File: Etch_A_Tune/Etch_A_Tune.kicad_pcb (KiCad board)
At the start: 2 copper layers, 114.2 x 101.6 mm, 21 parts, among them IC1 STM32H7A3ZIT6, IC2 TPS62063DSGR, IC3 BQ29702DSER, IC4 LM2775DSGR, IC5 BQ25170DSGR, IC6 TLV320DAC3100IRHBR, J1 TSM-115-01-T-DV-P-TR, J2 TSM-110-01-T-DV-P, J3 UJ20-C-H-G-MSMT-2-P16-TR, J4 TSM-117-01-F-DV-P-TR, J5 TSM-108-01-L-DV-A-P-TR, U1 1042P, U2 RIC11-31S10K2-GSMT, U3 RIC11-31S10K2-GSMT

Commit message: Schematic Update
Fixed component Footprints and added new switches/rotary encoders. Wired and placed bypass capacitors for most devices. Removed 5V boost converter because external DAC is no longer being utilized. Placed uC onto board design and implemented charging through USB-C connector.
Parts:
- removed IC2: TPS62063DSGR, SamacSys:SON50P200X200X80-9N
- removed IC3: BQ29702DSER, SamacSys:TPS3710QDSERQ1
- removed IC4: LM2775DSGR, SamacSys:SON50P200X200X80-9N
- removed IC5: BQ25170DSGR, SamacSys:SON50P200X200X80-9N
- removed IC6: TLV320DAC3100IRHBR, SamacSys:QFN50P500X500X100-33N-D
- removed J1: TSM-115-01-T-DV-P-TR, SamacSys:TSM-115-YY-ZZZ-DV-P-TR
- removed J3: UJ20-C-H-G-MSMT-2-P16-TR, SamacSys:UJ20CHGMSMT2P16TR
- removed J4: TSM-117-01-F-DV-P-TR, SamacSys:TSM-117-YY-ZZZ-DV-P-TR
- removed J5: TSM-108-01-L-DV-A-P-TR, SamacSys:TSM-108-YY-ZZZ-DV-A-P-TR
- removed J?: SJ2-35853A-SMT-TR, SamacSys:SJ235853ASMTTR
- removed U2: RIC11-31S10K2-GSMT, SamacSys:RIC1131S10K2GSMT
- added BT1: 1042P, BQ25170DSGR:BAT_1042P, B.Cu at (134.0, 50.0)
- added MT1: RIC11-31S15D7-GSMT, BQ25170DSGR:XDCR_RIC11-31S15D7-GSMT, F.Cu at (311.5, 76.5)
- added MT2: RIC11-31S15D7-GSMT, BQ25170DSGR:XDCR_RIC11-31S15D7-GSMT, F.Cu at (397.5, 76.5)
- added TP1: TestPoint, TestPoint:TestPoint_Pad_D1.0mm, F.Cu at (330.6, 37.5)
- added TP10: TestPoint, TestPoint:TestPoint_Pad_D1.0mm, F.Cu at (338.0, 46.1)
- added TP11: TestPoint, TestPoint:TestPoint_Pad_D1.0mm, F.Cu at (341.1, 37.0)
- added TP12: TestPoint, TestPoint:TestPoint_Pad_D1.0mm, F.Cu at (341.1, 40.0)
- added TP13: TestPoint, TestPoint:TestPoint_Pad_D1.0mm, F.Cu at (341.1, 43.0)
- added TP2: TestPoint, TestPoint:TestPoint_Pad_D1.0mm, F.Cu at (330.6, 44.5)
- added TP3: TestPoint, TestPoint:TestPoint_Pad_D1.0mm, F.Cu at (330.1, 41.0)
- added TP4: TestPoint, TestPoint:TestPoint_Pad_D1.0mm, F.Cu at (346.5, 44.0)
- added TP5: TestPoint, TestPoint:TestPoint_Pad_D1.0mm, F.Cu at (346.1, 37.0)
- added TP6: TestPoint, TestPoint:TestPoint_Pad_D1.0mm, F.Cu at (346.1, 40.0)
- added TP7: TestPoint, TestPoint:TestPoint_Pad_D1.0mm, F.Cu at (338.0, 37.0)
- added TP8: TestPoint, TestPoint:TestPoint_Pad_D1.0mm, F.Cu at (338.0, 40.0)
- added TP9: TestPoint, TestPoint:TestPoint_Pad_D1.0mm, F.Cu at (338.0, 43.0)
- added U4: STM32H7A3ZIT6Q, BQ25170DSGR:LQFP-144-L, F.Cu at (132.2, 64.8)
- added U6: CSD16406Q3, BQ25170DSGR:TRANS_CSD16406Q3, F.Cu at (315.0, 99.2)
- added U7: CSD16406Q3, BQ25170DSGR:TRANS_CSD16406Q3, F.Cu at (315.0, 104.0)
- IC1: value STM32H7A3ZIT6 -> BQ25170DSGR; footprint SamacSys:QFP50P2200X2200X160-144N -> BQ25170DSGR:SON50P200X200X80-9N
- J2: value TSM-110-01-T-DV-P -> 2171790001; footprint SamacSys:TSM-110-YY-ZZZ-DV-P -> BQ25170DSGR:MOLEX_2171790001
- S1: footprint SamacSys:450404015514 -> BQ25170DSGR:450404015514
- S2, S3, S4, S5, S6: value PTS647SM70SMTR2LFS -> B3AL-1005P; footprint SamacSys:PTS647SM38SMTR2LFS -> BQ25170DSGR:B3AL1005P
- U1: value 1042P -> BQ297xy; footprint SamacSys:1042P -> Package_SON:WSON-6_1.5x1.5mm_P0.5mm; moved to F.Cu
- U3: value RIC11-31S10K2-GSMT -> TPS62063DSGR; footprint SamacSys:RIC1131S10K2GSMT -> BQ25170DSGR:DSG0008A
- moved S3 235.5 mm to (342.5, 85.0), turned to 90 degrees
- moved S4 235.4 mm to (352.5, 85.0), turned to 90 degrees
- moved S5 235.2 mm to (362.5, 85.0), turned to 90 degrees
- moved S6 234.6 mm to (372.0, 85.0), turned to 90 degrees
- moved U3 222.4 mm to (314.5, 107.8)
- moved U1 200.7 mm to (338.5, 111.2)
- moved IC1 191.1 mm to (333.0, 111.2)
- moved S2 187.1 mm to (332.5, 85.0), turned to 90 degrees
- moved J2 123.6 mm to (80.2, 43.2), turned to -90 degrees
- moved S1 63.0 mm to (185.0, 40.0)
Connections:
- IC1 pad 1: (no net) -> /Battery/USB_Power
- IC1 pad 2: (no net) -> Net-(IC1-ISET)
- IC1 pad 3: (no net) -> Net-(IC1-TS)
- IC1 pad 4: (no net) -> GND
- IC1 pad 5: (no net) -> /Battery/BAT_DIAG
- IC1 pad 6: (no net) -> /Battery/PG
- IC1 pad 7: (no net) -> GND
- IC1 pad 8: (no net) -> /Battery/Power
- IC1 pad 9: (no net) -> GND
- S1 pad 1: (no net) -> Net-(R1-Pad1)
- S1 pad 2: (no net) -> /Controllers/SlideSwitch
- S1 pad 3: (no net) -> GND
- S2 pad 1: (no net) -> /Controllers/SW1
- S2 pad 2: (no net) -> GND
- S3 pad 1: (no net) -> /Controllers/SW2
- S3 pad 2: (no net) -> GND
- S4 pad 1: (no net) -> /Controllers/SW3
- S4 pad 2: (no net) -> GND
- S5 pad 1: (no net) -> /Controllers/SW4
- S5 pad 2: (no net) -> GND
- S6 pad 1: (no net) -> /Controllers/SW5
- S6 pad 2: (no net) -> GND
- U1 pad 1: (no net) -> unconnected-(U1-NC-Pad1)
- U1 pad 2: (no net) -> Net-(U1-Cout)
- U1 pad 3: (no net) -> Net-(U1-Dout)
- U1 pad 4: (no net) -> GND
- U1 pad 5: (no net) -> Net-(U1-BAT)
- U3 pad 1: (no net) -> GND
- U3 pad 2: (no net) -> Net-(U3-SW)

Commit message: Etch A Tune V.02
Updated more foot prints and components onto bom, specifically SWD debug header and 1x14 pin header for touch and screen module. Added 4pin header for SD card reader.
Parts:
- removed U6, U7: CSD16406Q3, BQ25170DSGR:TRANS_CSD16406Q3
- added J1: RSM-114-02-T-S, BQ25170DSGR:SAMTEC_RSM-114-02-T-S, F.Cu at (81.0, 85.5)
- added J3: M20-7910542R, BQ25170DSGR:HARWIN_M20-7910542R, F.Cu at (149.9, 43.3)
- added J4: 2171790001, BQ25170DSGR:MOLEX_2171790001, F.Cu at (80.0, 43.5)
- added U2: CSD16406Q3, BQ25170DSGR:TRANS_CSD16406Q3, F.Cu at (105.5, 64.1)
- added U5: STM32H7A3ZIT6Q, BQ25170DSGR:LQFP-144-L, F.Cu at (135.8, 80.3)
- J2: value 2171790001 -> 91601-304ALF; footprint BQ25170DSGR:MOLEX_2171790001 -> BQ25170DSGR:AMPHENOL_91601-304ALF
- S1: value 450404015514 -> B3AL-1005P; footprint BQ25170DSGR:450404015514 -> BQ25170DSGR:B3AL1005P
- S6: value B3AL-1005P -> 450404015514; footprint BQ25170DSGR:B3AL1005P -> BQ25170DSGR:450404015514
- U3: value TPS62063DSGR -> CSD16406Q3; footprint BQ25170DSGR:DSG0008A -> BQ25170DSGR:TRANS_CSD16406Q3
- U4: value STM32H7A3ZIT6Q -> TPS62063DSGR; footprint BQ25170DSGR:LQFP-144-L -> BQ25170DSGR:DSG0008A
- moved IC1 238.6 mm to (103.0, 48.0)
- moved U1 238.6 mm to (108.5, 48.0)
- moved MT1 230.2 mm to (87.0, 127.5)
- moved MT2 223.8 mm to (179.5, 127.0)
- moved S5 216.2 mm to (150.5, 127.5)
- moved S4 215.2 mm to (141.5, 127.5)
- moved S3 214.3 mm to (132.5, 127.5)
- moved S2 213.3 mm to (123.5, 127.5)
- moved U3 208.4 mm to (110.8, 64.1), turned to 90 degrees
- moved S6 194.9 mm to (182.5, 39.5), turned to 0 degrees
- moved TP1 140.7 mm to (201.5, 93.5)
- moved TP11 140.7 mm to (211.9, 93.0)
- moved TP12 140.7 mm to (211.9, 96.0)
- moved TP13 140.7 mm to (211.9, 99.0)
- moved TP2 140.7 mm to (201.5, 100.5)
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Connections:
- S1 pad 1: Net-(R1-Pad1) -> /Controllers/SW1
- S1 pad 2: /Controllers/SlideSwitch -> GND
- S2 pad 1: /Controllers/SW1 -> /Controllers/SW2
- S3 pad 1: /Controllers/SW2 -> /Controllers/SW3
- S4 pad 1: /Controllers/SW3 -> /Controllers/SW4
- S5 pad 1: /Controllers/SW4 -> /Controllers/SW5
- S6 pad 1: /Controllers/SW5 -> Net-(R18-Pad1)
- S6 pad 2: GND -> /Controllers/SlideSwitch
- TP1 pad 1: /Battery/USB_Power -> GND
- TP2 pad 1: /Battery/Power -> /Battery/USB_Power
- TP3 pad 1: /Battery/PG -> /Battery/Power
- TP4 pad 1: GND -> /Battery/PG
- U3 pad 2: Net-(U3-SW) -> GND
- U3 pad 4: Net-(U3-FB) -> Net-(U1-Cout)
- U3 pad 5: /Power/Power -> Net-(TP6-Pad1)
- U3 pad 6: GND -> Net-(TP6-Pad1)
- U3 pad 7: /Power/Power -> Net-(TP6-Pad1)
- U3 pad 8: /Power/Power -> Net-(TP6-Pad1)
- U4 pad 1: unconnected-(U4A-PE2-Pad1) -> GND
- U4 pad 2: unconnected-(U4A-PE3-Pad2) -> Net-(U4-SW)
- U4 pad 3: unconnected-(U4A-PE4-Pad3) -> GND
- U4 pad 4: unconnected-(U4A-PE5-Pad4) -> Net-(U4-FB)
- U4 pad 5: unconnected-(U4A-PE6-Pad5) -> /Power/Power
- U4 pad 7: +3.3V -> /Power/Power
- U4 pad 8: +3.3V -> /Power/Power
- U4 pad 9: unconnected-(U4A-PC13-Pad9) -> GND
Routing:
- net /SD_SCK: track 0.00 -> 81.2 mm
- net /T_DIN: track 0.00 -> 80.7 mm
- net /T_DO: track 0.00 -> 72.8 mm
- net /T_IRQ: track 0.00 -> 66.5 mm
- net GND: track 0.00 -> 53.2 mm
- net +3.3V: track 0.00 -> 47.5 mm
- net /SD_MOSI: track 0.00 -> 45.0 mm
- net /SD_MISO: track 0.00 -> 44.8 mm
- net /Battery/USB_Power: track 0.00 -> 41.8 mm
- net /SD_CS: track 0.00 -> 41.7 mm
- net Net-(U1-Dout): track 0.00 -> 26.0 mm
- net Net-(U1-Cout): track 0.00 -> 20.4 mm
- net /Power/Power: track 0.00 -> 5.93 mm
- net Net-(TP6-Pad1): track 0.00 -> 1.95 mm
- net /Controllers/ROTA1: track 0.00 -> 1.33 mm

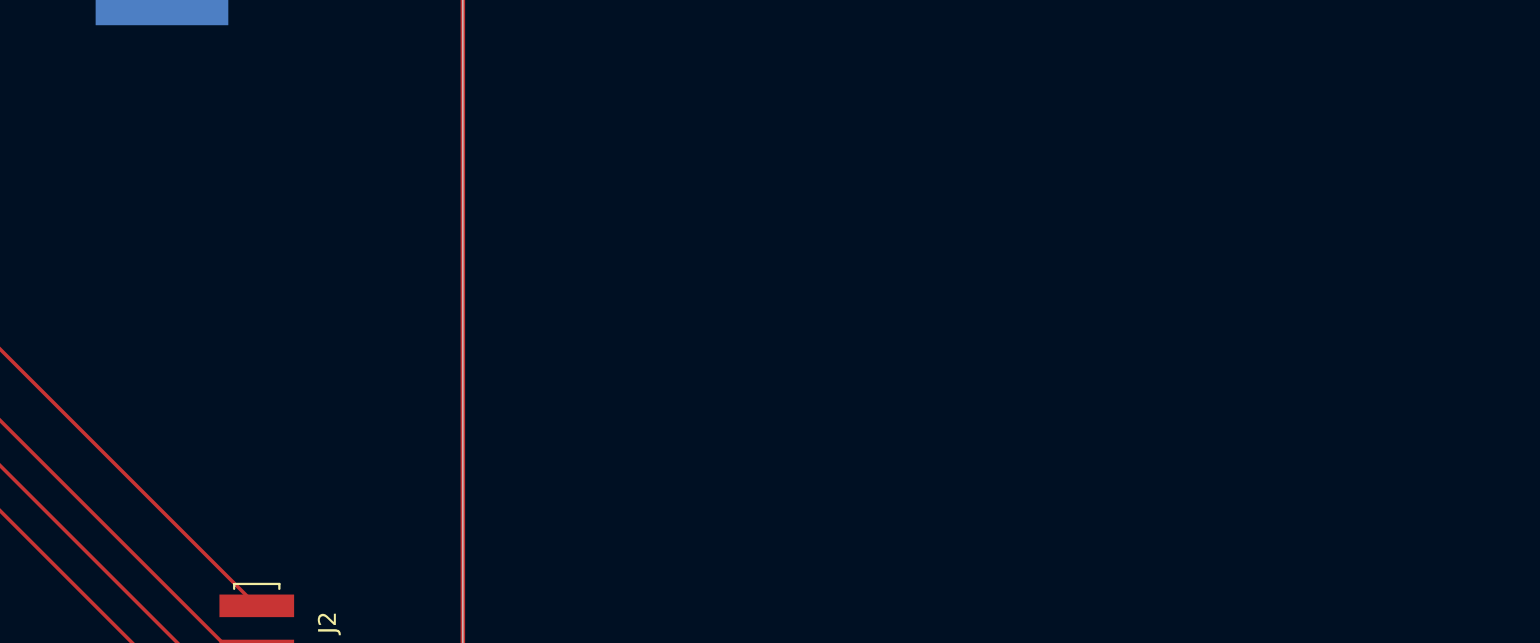
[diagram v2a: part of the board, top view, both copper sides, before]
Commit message: Updated parallel power supply
Updated USB and battery operation and added DAC output
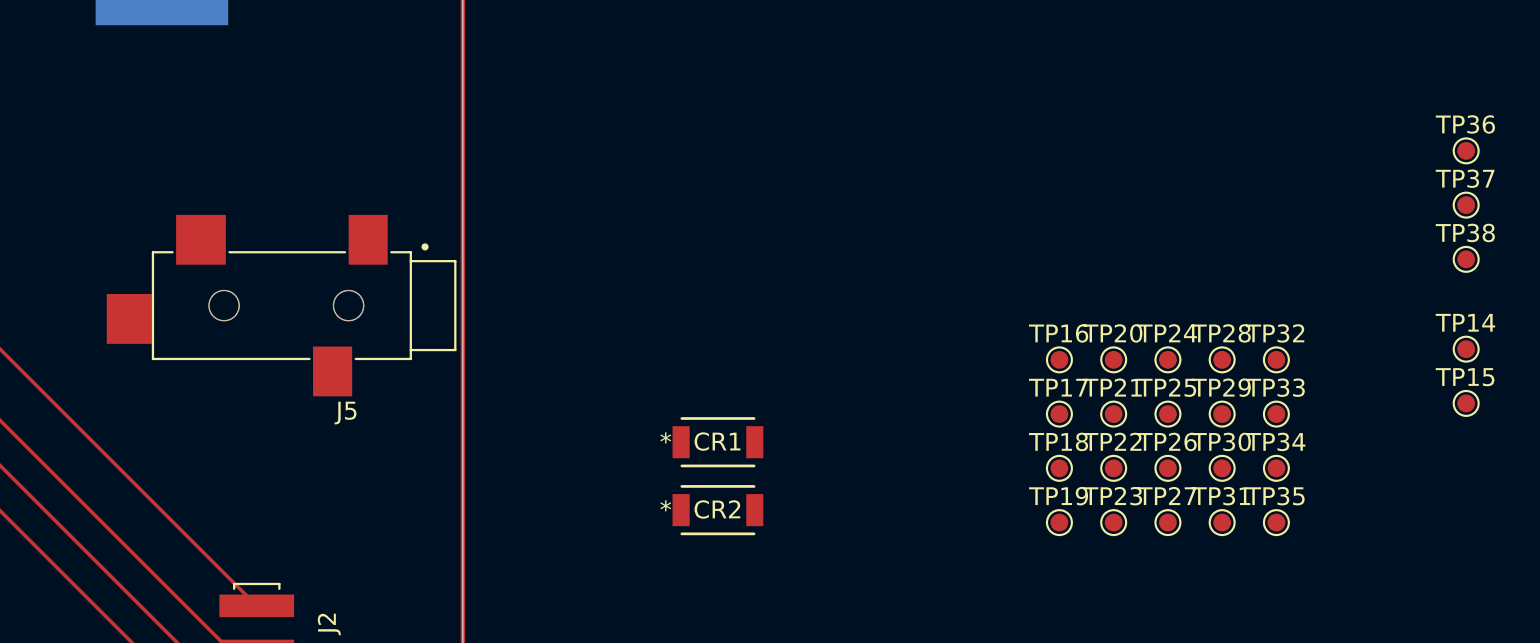
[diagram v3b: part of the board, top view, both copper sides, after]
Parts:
- added CR1: CMS06TE12L_Q_M, BQ25170DSGR:M-FLAT_TOS-L, F.Cu at (204.9, 76.7)
- added CR2: CMS06TE12L_Q_M, BQ25170DSGR:M-FLAT_TOS-L, F.Cu at (204.9, 80.5)
- added J5: SJ-3524-SMT-PI, BQ25170DSGR:CUI_SJ-3524-SMT-PI, F.Cu at (184.2, 69.0)
- added TP14: TestPoint, TestPoint:TestPoint_Pad_D1.0mm, F.Cu at (247.0, 71.5)
- added TP15: TestPoint, TestPoint:TestPoint_Pad_D1.0mm, F.Cu at (247.0, 74.5)
- added TP16: TestPoint, TestPoint:TestPoint_Pad_D1.0mm, F.Cu at (224.1, 72.0)
- added TP17: TestPoint, TestPoint:TestPoint_Pad_D1.0mm, F.Cu at (224.1, 75.1)
- added TP18: TestPoint, TestPoint:TestPoint_Pad_D1.0mm, F.Cu at (224.1, 78.2)
- added TP19: TestPoint, TestPoint:TestPoint_Pad_D1.0mm, F.Cu at (224.1, 81.2)
- added TP20: TestPoint, TestPoint:TestPoint_Pad_D1.0mm, F.Cu at (227.2, 72.0)
- added TP21: TestPoint, TestPoint:TestPoint_Pad_D1.0mm, F.Cu at (227.2, 75.1)
- added TP22: TestPoint, TestPoint:TestPoint_Pad_D1.0mm, F.Cu at (227.2, 78.2)
- added TP23: TestPoint, TestPoint:TestPoint_Pad_D1.0mm, F.Cu at (227.2, 81.2)
- added TP24: TestPoint, TestPoint:TestPoint_Pad_D1.0mm, F.Cu at (230.2, 72.0)
- added TP25: TestPoint, TestPoint:TestPoint_Pad_D1.0mm, F.Cu at (230.2, 75.1)
- added TP26: TestPoint, TestPoint:TestPoint_Pad_D1.0mm, F.Cu at (230.2, 78.2)
- added TP27: TestPoint, TestPoint:TestPoint_Pad_D1.0mm, F.Cu at (230.2, 81.2)
- added TP28: TestPoint, TestPoint:TestPoint_Pad_D1.0mm, F.Cu at (233.3, 72.0)
- added TP29: TestPoint, TestPoint:TestPoint_Pad_D1.0mm, F.Cu at (233.3, 75.1)
- added TP30: TestPoint, TestPoint:TestPoint_Pad_D1.0mm, F.Cu at (233.3, 78.2)
- added TP31: TestPoint, TestPoint:TestPoint_Pad_D1.0mm, F.Cu at (233.3, 81.2)
- added TP32: TestPoint, TestPoint:TestPoint_Pad_D1.0mm, F.Cu at (236.3, 72.0)
- added TP33: TestPoint, TestPoint:TestPoint_Pad_D1.0mm, F.Cu at (236.3, 75.1)
- added TP34: TestPoint, TestPoint:TestPoint_Pad_D1.0mm, F.Cu at (236.3, 78.2)
- added TP35: TestPoint, TestPoint:TestPoint_Pad_D1.0mm, F.Cu at (236.3, 81.2)
- added TP36: TestPoint, TestPoint:TestPoint_Pad_D1.0mm, F.Cu at (247.0, 60.3)
- added TP37: TestPoint, TestPoint:TestPoint_Pad_D1.0mm, F.Cu at (247.0, 63.4)
- added TP38: TestPoint, TestPoint:TestPoint_Pad_D1.0mm, F.Cu at (247.0, 66.4)
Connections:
- net /Battery/USB_Power renamed /Battery/USB_POWER
- net /Power/Power renamed Net-(U4-AVIN)
- net Net-(U1-Cout) renamed /Battery/CHARGE_GATE
- net Net-(U1-Dout) renamed /Battery/DISCHARGE_GATE
- BT1 pad P: /Battery/Power -> /Battery/BAT_V_SENSE
- IC1 pad 8: /Battery/Power -> /Battery/BAT_V_SENSE
- TP3 pad 1: /Battery/Power -> /Battery/BAT_V_SENSE
- U5 pad 112: unconnected-(U5B-PD0-Pad112) -> /Controllers/ROTP1
- U5 pad 113: unconnected-(U5B-PD1-Pad113) -> /Controllers/ROTB1
- U5 pad 114: unconnected-(U5B-PD2-Pad114) -> /Controllers/ROTA1
- U5 pad 115: unconnected-(U5B-PD3-Pad115) -> /Controllers/ROTP2
- U5 pad 116: unconnected-(U5B-PD4-Pad116) -> /Controllers/ROTB2
- U5 pad 117: unconnected-(U5B-PD5-Pad117) -> /Controllers/ROTA2
- U5 pad 118: unconnected-(U5B-VSS-Pad118) -> GND
- U5 pad 120: unconnected-(U5B-PD6-Pad120) -> /Controllers/SW1
- U5 pad 121: unconnected-(U5B-PD7-Pad121) -> /Controllers/SW2
- U5 pad 122: unconnected-(U5B-PG9-Pad122) -> /Controllers/SW3
- U5 pad 123: unconnected-(U5B-PG10-Pad123) -> /Controllers/SW4
- U5 pad 124: unconnected-(U5B-PG11-Pad124) -> /Controllers/SW5
- U5 pad 125: unconnected-(U5B-PG12-Pad125) -> /Controllers/SlideSwitch
- U5 pad 126: unconnected-(U5B-PG13-Pad126) -> /Battery/BAT_DIAG
- U5 pad 127: unconnected-(U5B-PG14-Pad127) -> /Battery/PG
- U5 pad 40: unconnected-(U5A-PA3-Pad40) -> /Battery/BAT_V_SENSE
- U5 pad 43: /CS -> /Microcontroller/DAC_OUT
- U5 pad 47: /RESET -> /CS
- U5 pad 48: /DC/RS -> /RESET
- U5 pad 49: /LED -> /DC/RS
- U5 pad 50: unconnected-(U5A-PB1-Pad50) -> /LED

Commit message: Final Layout before routing
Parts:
- removed J3: M20-7910542R, BQ25170DSGR:HARWIN_M20-7910542R
- removed TP35: TestPoint, TestPoint:TestPoint_Pad_D1.0mm
- added C1: 1uF, Capacitor_SMD:C_0603_1608Metric, F.Cu at (169.0, 117.3)
- added C2: 1uF, Capacitor_SMD:C_0603_1608Metric, F.Cu at (171.6, 117.3)
- added C3: .1uF, Capacitor_SMD:C_0603_1608Metric, F.Cu at (174.1, 117.3)
- added C4: 10uF, Capacitor_SMD:C_0603_1608Metric, F.Cu at (166.5, 24.7)
- added C5: 22pF, Capacitor_SMD:C_0603_1608Metric, F.Cu at (160.5, 29.7)
- added C6: 100nF, Capacitor_SMD:C_0603_1608Metric, F.Cu at (156.0, 105.5)
- added C8: 330uF, Capacitor_SMD:C_0603_1608Metric, F.Cu at (157.0, 117.3)
- added C9: 10uF, Capacitor_SMD:C_0603_1608Metric, F.Cu at (174.1, 111.3)
- added D1: 150060GS75000, LED_SMD:LED_0603_1608Metric, F.Cu at (160.5, 105.5)
- added D2: 150060GS75000, LED_SMD:LED_0603_1608Metric, F.Cu at (153.4, 105.5)
- added J6: 6130XX243121_613064243121, BQ25170DSGR:613064243121, F.Cu at (80.7, 22.6)
- added J7: 3220-10-0300-00, BQ25170DSGR:CNC_3220-10-0300-00, F.Cu at (22.6, 89.3)
- added L1: 1UH, Inductor_SMD:L_1210_3225Metric, F.Cu at (156.5, 24.7)
- added R1: 24k, Resistor_SMD:R_0603_1608Metric, F.Cu at (176.6, 117.3)
- added R10: 10k, Resistor_SMD:R_0603_1608Metric, B.Cu at (30.0, 98.7)
- added R11: 10k, Resistor_SMD:R_0603_1608Metric, B.Cu at (62.0, 106.7)
- added R12: 10k, Resistor_SMD:R_0603_1608Metric, B.Cu at (72.0, 106.7)
- added R13: 10k, Resistor_SMD:R_0603_1608Metric, F.Cu at (174.1, 101.2)
- added R14: 10k, Resistor_SMD:R_0603_1608Metric, F.Cu at (176.6, 101.2)
- added R15: 10k, Resistor_SMD:R_0603_1608Metric, B.Cu at (118.5, 98.7)
- added R16: 10k, Resistor_SMD:R_0603_1608Metric, B.Cu at (82.0, 106.7)
- added R17: 10k, Resistor_SMD:R_0603_1608Metric, B.Cu at (92.0, 106.7)
- added R18: 10k, Resistor_SMD:R_0603_1608Metric, F.Cu at (176.6, 97.2)
- added R19: 10k, Resistor_SMD:R_0603_1608Metric, F.Cu at (181.1, 105.2)
- added R2: 604, Resistor_SMD:R_0603_1608Metric, F.Cu at (179.1, 117.3)
- added R20: 10, Resistor_SMD:R_0603_1608Metric, F.Cu at (181.6, 111.3)
- added R21: 10, Resistor_SMD:R_0603_1608Metric, F.Cu at (183.6, 105.2)
- added R22: 5.1k, Resistor_SMD:R_0603_1608Metric, F.Cu at (159.5, 117.3)
- added R23: 5.1k, Resistor_SMD:R_0603_1608Metric, F.Cu at (33.5, 30.2)
- added R24: 0, Resistor_SMD:R_0603_1608Metric, F.Cu at (162.0, 117.3)
- added R25: 0, Resistor_SMD:R_0603_1608Metric, F.Cu at (164.5, 117.3)
- added R26: 0, Resistor_SMD:R_0603_1608Metric, F.Cu at (186.6, 117.3)
- added R27: 0, Resistor_SMD:R_0603_1608Metric, F.Cu at (184.1, 111.3)
- added R28: 0, Resistor_SMD:R_0603_1608Metric, F.Cu at (189.1, 117.3)
- added R29: 0, Resistor_SMD:R_0603_1608Metric, F.Cu at (186.6, 111.3)
- added R3: 330, Resistor_SMD:R_0603_1608Metric, F.Cu at (181.6, 117.3)
- added R30: 0, Resistor_SMD:R_0603_1608Metric, F.Cu at (189.1, 111.3)
- added R4: 2.2k, Resistor_SMD:R_0603_1608Metric, F.Cu at (184.1, 117.3)
- added R5: 360k, Resistor_SMD:R_0603_1608Metric, F.Cu at (160.5, 33.7)
- added R6: 180k, Resistor_SMD:R_0603_1608Metric, F.Cu at (160.5, 36.7)
- added R7: 10k, Resistor_SMD:R_0603_1608Metric, F.Cu at (169.0, 105.2)
- added R8: 10k, Resistor_SMD:R_0603_1608Metric, F.Cu at (171.6, 105.2)
- added R9: 10k, Resistor_SMD:R_0603_1608Metric, B.Cu at (52.0, 106.7)
- added TP39: TestPoint, TestPoint:TestPoint_Pad_D1.0mm, F.Cu at (219.0, 57.2)
- J1: value RSM-114-02-T-S -> 75915-414LF; footprint BQ25170DSGR:SAMTEC_RSM-114-02-T-S -> BQ25170DSGR:75915414LF
- moved U2 86.6 mm to (190.7, 48.6), turned to 180 degrees
- moved U3 82.5 mm to (190.7, 43.3), turned to 180 degrees
- moved J1 77.8 mm to (22.0, 34.8)
- moved IC1 71.7 mm to (174.6, 51.1), turned to 90 degrees
- moved U1 66.1 mm to (174.6, 45.6), turned to 90 degrees
- moved S1 65.8 mm to (52.0, 106.7)
- moved J2 65.7 mm to (126.0, 50.8), turned to 90 degrees
- moved S2 64.9 mm to (62.0, 106.7)
- moved MT2 64.2 mm to (118.5, 106.7)
- moved S3 63.9 mm to (72.0, 106.7)
- moved S4 63.0 mm to (82.0, 106.7)
- moved U5 62.9 mm to (73.5, 71.2)
- moved S5 62.1 mm to (92.0, 106.7)
- moved J5 61.7 mm to (125.7, 88.7)
- moved BT1 60.8 mm to (73.5, 43.7)
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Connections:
- BT1 pad N: GND -> Net-(U1-VSS)
- BT1 pad P: /Battery/BAT_V_SENSE -> /Battery/PACK+
- CR1 pad 1: /Battery/BAT_V_SENSE -> Net-(CR1-Pad1)
- CR2 pad 1: /Battery/USB_POWER -> Net-(CR2-Pad1)
- IC1 pad 1: /Battery/USB_POWER -> Net-(IC1-IN)
- IC1 pad 4: GND -> +3.3V
- IC1 pad 7: GND -> +3.3V
- IC1 pad 8: /Battery/BAT_V_SENSE -> /Battery/PACK+
- IC1 pad 9: GND -> +3.3V
- J1 pad 13: GND -> +3.3V
- J4 pad A1B12: GND -> +3.3V
- J4 pad A5: unconnected-(J4-CC1-PadA5) -> Net-(J4-CC1)
- J4 pad B1A12: GND -> +3.3V
- J4 pad B5: unconnected-(J4-CC2-PadB5) -> Net-(J4-CC2)
- J5 pad 1: unconnected-(J5-Pad1) -> +3.3V
- J5 pad 2: unconnected-(J5-Pad2) -> Net-(J5-Pad2)
- J5 pad 3: unconnected-(J5-Pad3) -> Net-(J5-Pad3)
- MT1 pad C: GND -> +3.3V
- MT1 pad D: GND -> +3.3V
- MT2 pad C: GND -> +3.3V
- MT2 pad D: GND -> +3.3V
- S1 pad 2: GND -> +3.3V
- S2 pad 2: GND -> +3.3V
- S3 pad 2: GND -> +3.3V
- S4 pad 2: GND -> +3.3V
- S5 pad 2: GND -> +3.3V
- S6 pad 3: GND -> +3.3V
- TP1 pad 1: GND -> +3.3V
- TP3 pad 1: /Battery/BAT_V_SENSE -> /Battery/PACK+
- TP32 pad 1: /SWRESET -> /SWDIO
- TP33 pad 1: /SWDIO -> /SWCLK
- TP34 pad 1: /SWCLK -> /SWO
- TP37 pad 1: /Battery/BAT_V_SENSE -> /Battery/PACK+
- TP38 pad 1: +3.3V -> Net-(C5-Pad1)
- U1 pad 4: GND -> Net-(U1-VSS)
- U2 pad 1: GND -> Net-(U1-VSS)
- U2 pad 2: GND -> Net-(U1-VSS)
- U2 pad 3: GND -> Net-(U1-VSS)
- U3 pad 1: GND -> +3.3V
- U3 pad 2: GND -> +3.3V
- U3 pad 3: GND -> +3.3V
- U4 pad 1: GND -> +3.3V
- U4 pad 3: GND -> +3.3V
- U4 pad 6: GND -> +3.3V
- U4 pad 9: GND -> +3.3V
- U5 pad 1: unconnected-(U5A-PE2-Pad1) -> Net-(U5A-PE2)
- U5 pad 100: unconnected-(U5B-PA11-Pad100) -> PA11
- U5 pad 101: unconnected-(U5B-PA12-Pad101) -> PA12
- U5 pad 102: unconnected-(U5B-PA13-Pad102) -> /SWDIO
- U5 pad 107: unconnected-(U5B-PA14-Pad107) -> /SWCLK
- U5 pad 118: GND -> +3.3V
- U5 pad 12: GND -> +3.3V
- U5 pad 130: unconnected-(U5B-PB3-Pad130) -> /SWO
- U5 pad 131: unconnected-(U5B-PB4-Pad131) -> PB4
- U5 pad 132: unconnected-(U5B-PB5-Pad132) -> PB5
- U5 pad 133: unconnected-(U5B-PB6-Pad133) -> PB6
- U5 pad 134: unconnected-(U5B-PB7-Pad134) -> PB7
- U5 pad 136: unconnected-(U5B-PB8-Pad136) -> PB8
- U5 pad 137: unconnected-(U5B-PB9-Pad137) -> PB9
- U5 pad 138: unconnected-(U5B-PE0-Pad138) -> PE0
- U5 pad 139: unconnected-(U5B-PE1-Pad139) -> PE1
- U5 pad 18: GND -> +3.3V
- U5 pad 2: unconnected-(U5A-PE3-Pad2) -> PE3
- U5 pad 20: unconnected-(U5A-PF6-Pad20) -> PF6
- U5 pad 21: unconnected-(U5A-PF7-Pad21) -> PF7
- U5 pad 22: unconnected-(U5A-PF8-Pad22) -> PF8
- U5 pad 23: unconnected-(U5A-PF9-Pad23) -> PF9
- U5 pad 24: unconnected-(U5A-PF10-Pad24) -> PF10
- U5 pad 27: /SWRESET -> /nRESET
- U5 pad 28: unconnected-(U5A-PC0-Pad28) -> PC0
- U5 pad 29: unconnected-(U5A-PC1-Pad29) -> PC1
- U5 pad 3: unconnected-(U5A-PE4-Pad3) -> PE4
- U5 pad 30: unconnected-(U5A-PC2_C-Pad30) -> PC2_C
- U5 pad 31: unconnected-(U5A-PC3_C-Pad31) -> PC3_C
- U5 pad 33: GND -> +3.3V
- U5 pad 34: GND -> +3.3V
- U5 pad 37: unconnected-(U5A-PA0-Pad37) -> PA0
- U5 pad 38: unconnected-(U5A-PA1-Pad38) -> PA1
- U5 pad 39: unconnected-(U5A-PA2-Pad39) -> PA2
- U5 pad 4: unconnected-(U5A-PE5-Pad4) -> PE5
- U5 pad 41: GND -> +3.3V
- U5 pad 5: unconnected-(U5A-PE6-Pad5) -> PE6
- U5 pad 51: unconnected-(U5A-PB2-Pad51) -> PB2
- U5 pad 52: unconnected-(U5A-PF11-Pad52) -> PF11
- U5 pad 53: unconnected-(U5A-PF14-Pad53) -> PF14
- U5 pad 54: unconnected-(U5A-PF15-Pad54) -> PF15
- U5 pad 55: GND -> +3.3V
- U5 pad 57: unconnected-(U5A-PE7-Pad57) -> PE7
- U5 pad 58: unconnected-(U5A-PE8-Pad58) -> PE8
- U5 pad 59: unconnected-(U5A-PE9-Pad59) -> PE9
- U5 pad 6: GND -> +3.3V
- U5 pad 60: unconnected-(U5A-PE10-Pad60) -> PE10
- U5 pad 61: unconnected-(U5A-PE11-Pad61) -> PE11
- U5 pad 62: unconnected-(U5A-PE12-Pad62) -> PE12
- U5 pad 63: unconnected-(U5A-PE13-Pad63) -> PE13
- U5 pad 64: unconnected-(U5A-PE14-Pad64) -> PE14
- U5 pad 65: unconnected-(U5A-PE15-Pad65) -> PE15
- U5 pad 66: unconnected-(U5A-PB10-Pad66) -> PB10
- U5 pad 67: unconnected-(U5A-PB11-Pad67) -> PB11
- U5 pad 69: GND -> +3.3V
- U5 pad 77: unconnected-(U5B-PD9-Pad77) -> PD9
- U5 pad 78: unconnected-(U5B-PD10-Pad78) -> PD10
- U5 pad 81: unconnected-(U5B-PD11-Pad81) -> PD11
- U5 pad 82: unconnected-(U5B-PD12-Pad82) -> PD12
- U5 pad 83: unconnected-(U5B-PD13-Pad83) -> PD13
- U5 pad 84: unconnected-(U5B-PD14-Pad84) -> PD14
- U5 pad 85: unconnected-(U5B-PD15-Pad85) -> PD15
- U5 pad 86: unconnected-(U5B-PG6-Pad86) -> PG6
- U5 pad 87: unconnected-(U5B-PG7-Pad87) -> PG7
- U5 pad 88: unconnected-(U5B-PG8-Pad88) -> PG8
- U5 pad 9: unconnected-(U5A-PC13-Pad9) -> PC13
- U5 pad 93: unconnected-(U5B-PC6-Pad93) -> PC6
- U5 pad 94: unconnected-(U5B-PC7-Pad94) -> PC7
- U5 pad 95: unconnected-(U5B-PC8-Pad95) -> PC8
- U5 pad 96: unconnected-(U5B-PC9-Pad96) -> PC9
- U5 pad 97: unconnected-(U5B-PA8-Pad97) -> PA8
- U5 pad 98: unconnected-(U5B-PA9-Pad98) -> PA9
- U5 pad 99: unconnected-(U5B-PA10-Pad99) -> PA10
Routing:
- net /SD_SCK: track 81.2 -> 0.00 mm
- net /T_DIN: track 80.7 -> 0.00 mm
- net /T_DO: track 72.8 -> 0.00 mm
- net /T_IRQ: track 66.5 -> 0.00 mm
- net GND: track 53.2 -> 0.00 mm
- net +3.3V: track 47.5 -> 2.26 mm
- net /SD_MOSI: track 45.0 -> 0.00 mm
- net /SD_MISO: track 44.8 -> 0.00 mm
- net /Battery/USB_POWER: track 41.8 -> 0.00 mm
- net /SD_CS: track 41.7 -> 0.00 mm
- net /Battery/DISCHARGE_GATE: track 26.0 -> 0.00 mm
- net /Battery/CHARGE_GATE: track 20.4 -> 0.00 mm
- net Net-(U4-AVIN): track 5.93 -> 0.00 mm
- net /Controllers/ROTA1: track 1.33 -> 0.00 mm
- net Net-(TP6-Pad1): track 1.95 -> 1.30 mm
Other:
- board size 114.2 x 101.6 mm -> 114.5 x 99.7 mm
- copper layers 2 -> 4
